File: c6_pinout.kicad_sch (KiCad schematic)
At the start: 18 parts, among them J4 Conn_01x08_Socket, J5 Conn_01x06_Socket, J6 Conn_01x04, J7 Conn_01x10_Socket, J8 Conn_01x08_Socket, J9 Conn_02x03_Counter_Clockwise, U4 ESP32-C6-WROOM-1-N8

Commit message: pcb component layout
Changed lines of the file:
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@@
+		)
+	)
+	(hierarchical_label "EN"
+		(shape input)
+		(at 182.88 40.64 180)
+		(effects
+			(font
+				(size 1.27 1.27)
+			)
+			(justify right)
 		)
 	)

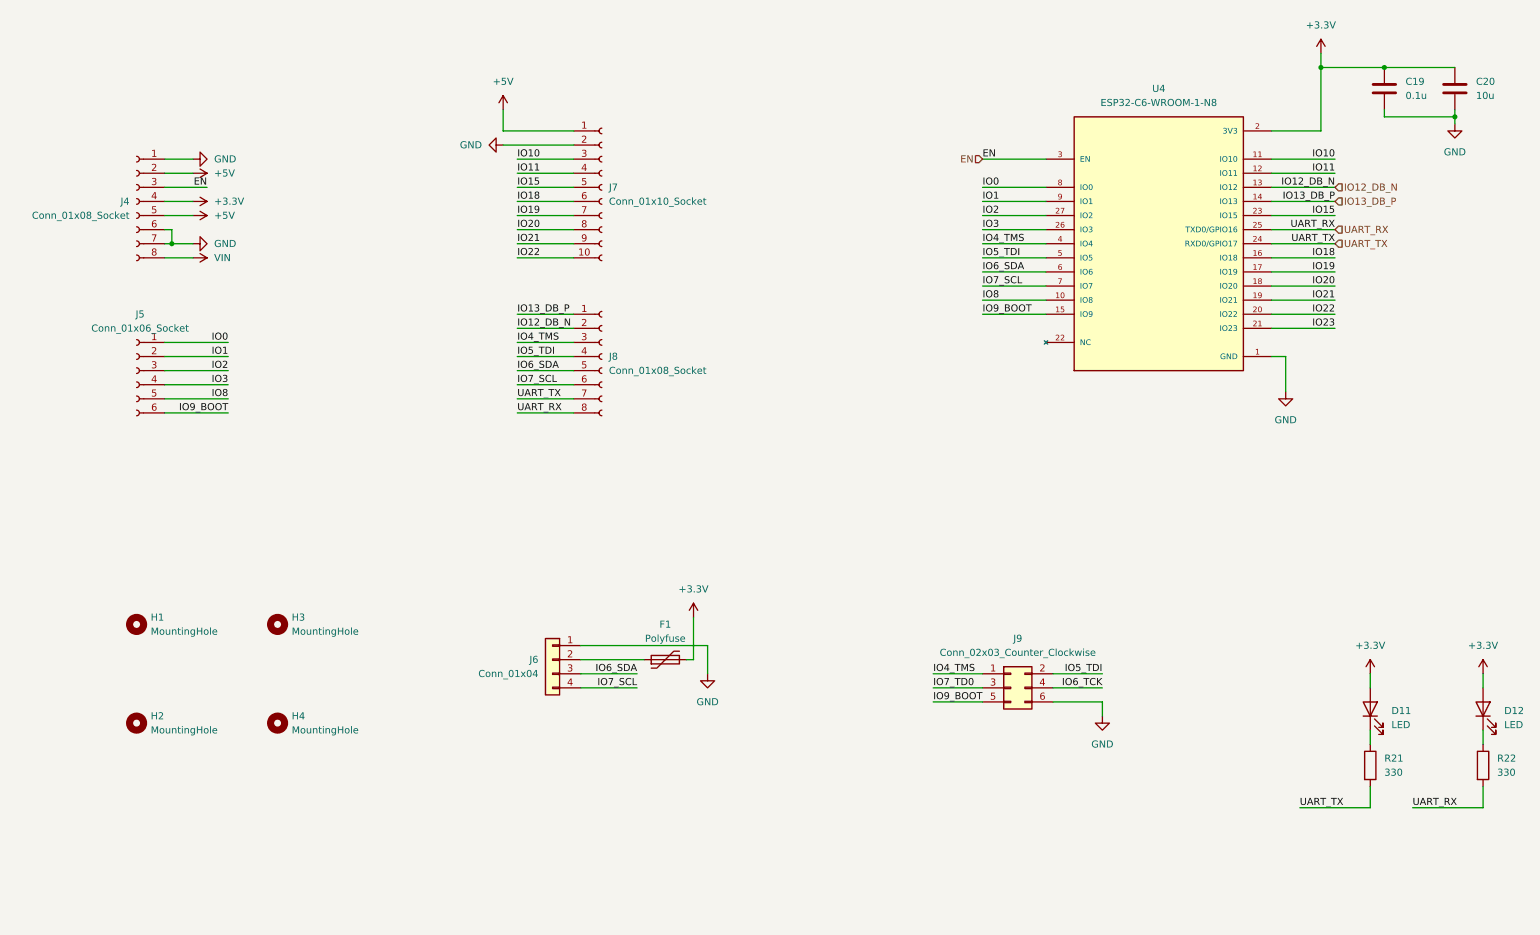
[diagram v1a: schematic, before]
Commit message: layout + power pin traces
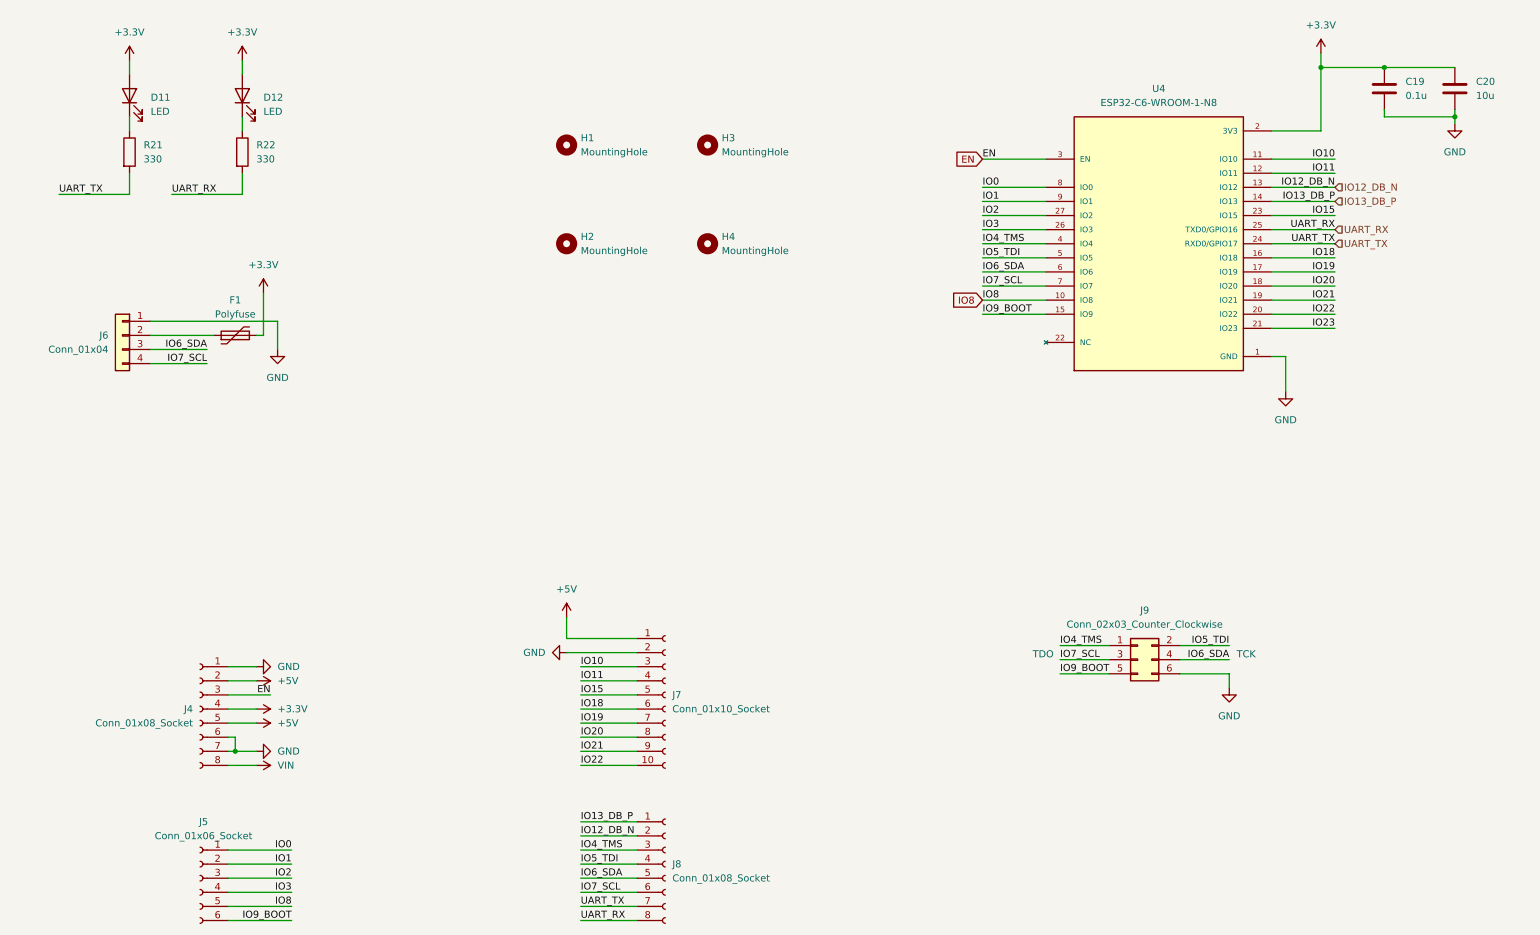
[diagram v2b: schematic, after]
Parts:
- J6: footprint Connector_JST:JST_XH_S4B-XH-A-1_1x04_P2.50mm_Horizontal -> uno-esp:CONN_SM04B-SRSS-TB_JST
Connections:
- net IO6_TCK is gone; now on net IO6_SDA: J9.4 (Pin_4)
- net IO7_TD0 is gone; now on net IO7_SCL: J9.3 (Pin_3)
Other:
- note added: "TCK"
- note added: "TDO"
- moved on the sheet: D11, D12, F1, H1, H2, H3, H4, J4, J5, J6, J7, J8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

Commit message: final tracing + pcb layers + colors
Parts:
- removed J8: Conn_01x08_Socket, Connector_PinSocket_1.27mm:PinSocket_1x08_P1.27mm_Vertical, symbol Connector:Conn_01x08_Socket
- removed J9: Conn_02x03_Counter_Clockwise, Connector_PinHeader_2.00mm:PinHeader_2x03_P2.00mm_Vertical, symbol Connector_Generic:Conn_02x03_Odd_Even
- added D10: PMEG6020AELR, Diode_SMD:Nexperia_CFP3_SOD-123W, symbol Diode:PMEG6020AELR
- added J8: Conn_01x06_Socket, Connector_PinSocket_1.27mm:PinSocket_1x06_P1.27mm_Vertical, symbol Connector:Conn_01x06_Socket
- added R6: 0, Resistor_SMD:R_0402_1005Metric_Pad0.72x0.64mm_HandSolder, symbol Device:R
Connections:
- net +3.3V: now also R6.1, R6.2
- net IO4_TMS: now also J8.1 (Pin_1)
- net IO5_TDI: now also J8.2 (Pin_2)
- net IO6_SDA: now also J8.3 (Pin_3)
- net IO7_SCL: now also J8.4 (Pin_4)
- net UART_RX: now also J8.6 (Pin_6)
- net UART_TX: now also J8.5 (Pin_5)
- net VIN: now also D10.1 (K); no longer J4.8 (Pin_8)
- net IO12_DB_N renamed DB_N
- net IO13_DB_P renamed DB_P
- new net: D10.2 (A), J4.8 (Pin_8)
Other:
- note removed: "TCK"
- note removed: "TDO"

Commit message: Refinement to pcb and schematic layout
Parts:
- removed H1, H2, H3, H4: MountingHole, MountingHole:MountingHole_2.1mm, symbol Mechanical:MountingHole
- removed J7: Conn_01x10_Socket, Connector_PinSocket_2.00mm:PinSocket_1x10_P2.00mm_Vertical, symbol Connector:Conn_01x10_Socket
- added J9: Conn_01x09_Socket, Connector_PinSocket_2.00mm:PinSocket_1x09_P2.00mm_Vertical, symbol Connector:Conn_01x09_Socket
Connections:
- net GND: now also J9.1 (Pin_1)
- net IO10: now also J9.2 (Pin_2)
- net IO11: now also J9.3 (Pin_3)
- net IO15: now also J9.4 (Pin_4)
- net IO18: now also J9.5 (Pin_5)
- net IO19: now also J9.6 (Pin_6)
- net IO20: now also J9.7 (Pin_7)
- net IO21: now also J9.8 (Pin_8)
- net IO22: now also J9.9 (Pin_9)
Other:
- title: (none) -> ESP32-C6 Dev Board
- moved on the sheet: C19, C20, D10, D11, D12, F1, J4, J5, J6, J8, R21, R22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
